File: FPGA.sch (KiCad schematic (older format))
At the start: 55 parts, among them J1 Conn_02x07_Odd_Even, J2 26642801RP2, U3 XC7A100T-FTG256, U4 S25FL1, U5 SiT2024B, U6 AS6C1616

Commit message: Minor FPGA and MCU fixes
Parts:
- added C?: 100n, symbol Device:C
- U5: footprint Package_TO_SOT_SMD:SOT-23-5 -> Package_TO_SOT_SMD:SOT-23-5_HandSoldering
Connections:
- net +3V3: now also C?.2
- net GND: now also C?.1
- net done renamed DONE
- net program_b renamed PROGRAM_B
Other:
- moved on the sheet: U6
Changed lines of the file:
@@
 F 0 "U5" H 5183 4625 50  0000 C CNN
 F 1 "SiT2024B" H 5183 4534 50  0000 C CNN
-F 2 "Package_TO_SOT_SMD:SOT-23-5" H 5100 4500 50  0001 C CNN
+F 2 "Package_TO_SOT_SMD:SOT-23-5_HandSoldering" H 5100 4500 50  0001 C CNN
 F 3 "" H 5100 4500 50  0001 C CNN
 	1    5300 4550
@@
 	1    0    0    -1
 $EndComp
-Text Label 19250 3400 2    50   ~ 0
+Text Label 18300 4000 2    50   ~ 0
 SRAM_dio0
-Text Label 19250 3300 2    50   ~ 0
+Text Label 18300 3900 2    50   ~ 0
 SRAM_dio1
-Text Label 19250 3200 2    50   ~ 0
+Text Label 18300 3800 2    50   ~ 0
 SRAM_dio2
-Text Label 19250 3100 2    50   ~ 0
+Text Label 18300 3700 2    50   ~ 0
 SRAM_dio3
-Text Label 19250 3000 2    50   ~ 0
+Text Label 18300 3600 2    50   ~ 0
 SRAM_dio4
-Text Label 19250 2900 2    50   ~ 0
+Text Label 18300 3500 2    50   ~ 0
 SRAM_dio5
-Text Label 19250 2800 2    50   ~ 0
+Text Label 18300 3400 2    50   ~ 0
 SRAM_dio6
-Text Label 19250 2700 2    50   ~ 0
+Text Label 18300 3300 2    50   ~ 0
 SRAM_dio7
-Text Label 19250 2600 2    50   ~ 0
+Text Label 18300 3200 2    50   ~ 0
 SRAM_dio8
-Text Label 19250 2500 2    50   ~ 0
+Text Label 18300 3100 2    50   ~ 0
 SRAM_dio9
-Text Label 19250 2400 2    50   ~ 0
+Text Label 18300 3000 2    50   ~ 0
 SRAM_dio10
-Text Label 19250 2300 2    50   ~ 0
+Text Label 18300 2900 2    50   ~ 0
 SRAM_dio11
-Text Label 19250 2200 2    50   ~ 0
+Text Label 18300 2800 2    50   ~ 0
 SRAM_dio12
-Text Label 19250 2100 2    50   ~ 0
+Text Label 18300 2700 2    50   ~ 0
 SRAM_dio13
-Text Label 19250 2000 2    50   ~ 0
+Text Label 18300 2600 2    50   ~ 0
 SRAM_dio14
-Text Label 19250 1900 2    50   ~ 0
+Text Label 18300 2500 2    50   ~ 0
 SRAM_dio15
 Text Label 16650 2100 0    50   ~ 0
@@
 Text Label 16650 3600 0    50   ~ 0
 SRAM_dio15
-Text Label 20450 3800 0    50   ~ 0
+Text Label 19500 4400 0    50   ~ 0
 SRAM_a0
-Text Label 20450 3700 0    50   ~ 0
+Text Label 19500 4300 0    50   ~ 0
 SRAM_a1
-Text Label 20450 3600 0    50   ~ 0
+Text Label 19500 4200 0    50   ~ 0
 SRAM_a2
-Text Label 20450 3500 0    50   ~ 0
+Text Label 19500 4100 0    50   ~ 0
 SRAM_a3
-Text Label 20450 3400 0    50   ~ 0
+Text Label 19500 4000 0    50   ~ 0
 SRAM_a4
-Text Label 20450 3300 0    50   ~ 0
+Text Label 19500 3900 0    50   ~ 0
 SRAM_a5
-Text Label 20450 3200 0    50   ~ 0
+Text Label 19500 3800 0    50   ~ 0
 SRAM_a6
-Text Label 20450 3100 0    50   ~ 0
+Text Label 19500 3700 0    50   ~ 0
 SRAM_a7
-Text Label 20450 3000 0    50   ~ 0
+Text Label 19500 3600 0    50   ~ 0
 SRAM_a8
-Text Label 20450 2900 0    50   ~ 0
+Text Label 19500 3500 0    50   ~ 0
 SRAM_a9
-Text Label 20450 2800 0    50   ~ 0
+Text Label 19500 3400 0    50   ~ 0
 SRAM_a10
-Text Label 20450 2700 0    50   ~ 0
+Text Label 19500 3300 0    50   ~ 0
 SRAM_a11
-Text Label 20450 2600 0    50   ~ 0
+Text Label 19500 3200 0    50   ~ 0
 SRAM_a12
-Text Label 20450 2500 0    50   ~ 0
+Text Label 19500 3100 0    50   ~ 0
 SRAM_a13
-Text Label 20450 2400 0    50   ~ 0
+Text Label 19500 3000 0    50   ~ 0
 SRAM_a14
-Text Label 20450 2300 0    50   ~ 0
+Text Label 19500 2900 0    50   ~ 0
 SRAM_a15
-Text Label 20450 2200 0    50   ~ 0
+Text Label 19500 2800 0    50   ~ 0
 SRAM_a16
-Text Label 20450 2100 0    50   ~ 0
+Text Label 19500 2700 0    50   ~ 0
 SRAM_a17
-Text Label 20450 2000 0    50   ~ 0
+Text Label 19500 2600 0    50   ~ 0
 SRAM_a18
-Text Label 20450 1900 0    50   ~ 0
+Text Label 19500 2500 0    50   ~ 0
 SRAM_a19
 Text Label 16650 3700 0    50   ~ 0
@@
 L Memory_RAM:AS6C1616 U?
 U 1 1 5E505DC8
-P 19850 3000
+P 18900 3600
 AR Path="/5D7D43D9/5E0EF1ED/5E505DC8" Ref="U?"  Part="1"
 AR Path="/5D7D43D9/5E505DC8" Ref="U6"  Part="1"
-F 0 "U6" H 19600 4300 50  0000 C CNN
-F 1 "AS6C1616" H 20150 1700 50  0000 C CNN
-F 2 "Package_SO:TSOP-I-48_18.4x12mm_P0.5mm" H 20900 1650 50  0001 C CNN
-F 3 "https://www.alliancememory.com/wp-content/uploads/pdf/AS6C1616-TSOPI.pdf" H 19550 3450 50  0001 C CNN
-	1    19850 3000
-	1    0    0    -1
-$EndComp
-Text Label 19250 3600 2    50   ~ 0
+F 0 "U6" H 18650 4900 50  0000 C CNN
+F 1 "AS6C1616" H 19200 2300 50  0000 C CNN
+F 2 "Package_SO:TSOP-I-48_18.4x12mm_P0.5mm" H 19950 2250 50  0001 C CNN
+F 3 "https://www.alliancememory.com/wp-content/uploads/pdf/AS6C1616-TSOPI.pdf" H 18600 4050 50  0001 C CNN
+	1    18900 3600
+	1    0    0    -1
+$EndComp
+Text Label 18300 4200 2    50   ~ 0
 SRAM_oe#
-Text Label 19250 3700 2    50   ~ 0
+Text Label 18300 4300 2    50   ~ 0
 SRAM_we#
-Text Label 19250 3800 2    50   ~ 0
+Text Label 18300 4400 2    50   ~ 0
 SRAM_ce#
-Text Label 19250 3900 2    50   ~ 0
+Text Label 18300 4500 2    50   ~ 0
 SRAM_ce2
-Text Label 19250 4000 2    50   ~ 0
+Text Label 18300 4600 2    50   ~ 0
 SRAM_ub#
-Text Label 19250 4100 2    50   ~ 0
+Text Label 18300 4700 2    50   ~ 0
 SRAM_lb#
 Text Label 16650 5700 0    50   ~ 0
@@
 SRAM_lb#
 Wire Wire Line
-	19850 1400 19850 1600
+	18900 2000 18900 2100
 $Comp
 L power:GND #PWR?
 U 1 1 5E505DDB
-P 19450 4450
+P 18500 5050
 AR Path="/5D7D43D9/5E0EF1ED/5E505DDB" Ref="#PWR?"  Part="1"
 AR Path="/5D7D43D9/5E505DDB" Ref="#PWR0126"  Part="1"
-F 0 "#PWR0126" H 19450 4200 50  0001 C CNN
-F 1 "GND" H 19455 4277 50  0000 C CNN
-F 2 "" H 19450 4450 50  0001 C CNN
-F 3 "" H 19450 4450 50  0001 C CNN
-	1    19450 4450
-	1    0    0    -1
-$EndComp
-Wire Wire Line
-	19850 4400 19750 4400
-Wire Wire Line
-	19450 4400 19450 4450
-Connection ~ 19750 4400
-Wire Wire Line
-	19750 4400 19450 4400
+F 0 "#PWR0126" H 18500 4800 50  0001 C CNN
+F 1 "GND" H 18505 4877 50  0000 C CNN
+F 2 "" H 18500 5050 50  0001 C CNN
+F 3 "" H 18500 5050 50  0001 C CNN
+	1    18500 5050
+	1    0    0    -1
+$EndComp
+Wire Wire Line
+	18900 5000 18800 5000
+Wire Wire Line
+	18500 5000 18500 5050
+Connection ~ 18800 5000
+Wire Wire Line
+	18800 5000 18500 5000
 NoConn ~ 16650 6300
 NoConn ~ 16650 6400
@@
 L power:+3V3 #PWR?
 U 1 1 5E505DED
-P 19850 1400
+P 18900 2000
 AR Path="/5D7D43D9/5E0EF1ED/5E505DED" Ref="#PWR?"  Part="1"
 AR Path="/5D7D43D9/5E505DED" Ref="#PWR0127"  Part="1"
-F 0 "#PWR0127" H 19850 1250 50  0001 C CNN
-F 1 "+3V3" H 19865 1573 50  0000 C CNN
-F 2 "" H 19850 1400 50  0001 C CNN
-F 3 "" H 19850 1400 50  0001 C CNN
-	1    19850 1400
+F 0 "#PWR0127" H 18900 1850 50  0001 C CNN
+F 1 "+3V3" H 18915 2173 50  0000 C CNN
+F 2 "" H 18900 2000 50  0001 C CNN
+F 3 "" H 18900 2000 50  0001 C CNN
+	1    18900 2000
 	1    0    0    -1
 $EndComp
@@
 Connection ~ -1500 1050
 Connection ~ -1500 1850
-Text GLabel -2600 1600 3    50   Input ~ 0
-done
 Wire Wire Line
 	-2600 1250 -2600 1600
 Connection ~ -2600 1250
-Text GLabel -3200 1600 3    50   Input ~ 0
-program_b
 Wire Wire Line
 	-3200 1600 -3200 1450
@@
 Text HLabel 6700 3400 0    50   Input ~ 0
 MISO
+Text HLabel -3200 1600 3    50   Input ~ 0
+PROGRAM_B
+Text HLabel -2600 1600 3    50   Input ~ 0
+DONE
+$Comp
+L Device:C C?
+U 1 1 60BCCCE6
+P 19250 2100
+F 0 "C?" V 18998 2100 50  0000 C CNN
+F 1 "100n" V 19089 2100 50  0000 C CNN
+F 2 "" H 19288 1950 50  0001 C CNN
+F 3 "~" H 19250 2100 50  0001 C CNN
+	1    19250 2100
+	0    1    1    0
+$EndComp
+Wire Wire Line
+	19100 2100 18900 2100
+Connection ~ 18900 2100
+Wire Wire Line
+	18900 2100 18900 2200
+$Comp
+L power:GND #PWR?
+U 1 1 60BE3158
+P 19550 2100
+F 0 "#PWR?" H 19550 1850 50  0001 C CNN
+F 1 "GND" H 19555 1927 50  0000 C CNN
+F 2 "" H 19550 2100 50  0001 C CNN
+F 3 "" H 19550 2100 50  0001 C CNN
+	1    19550 2100
+	1    0    0    -1
+$EndComp
+Wire Wire Line
+	19550 2100 19400 2100
 $EndSCHEMATC

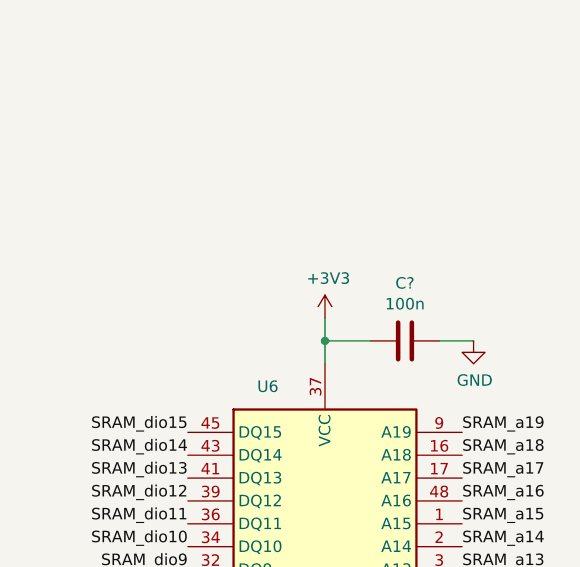
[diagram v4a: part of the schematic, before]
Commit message: Add various footprints
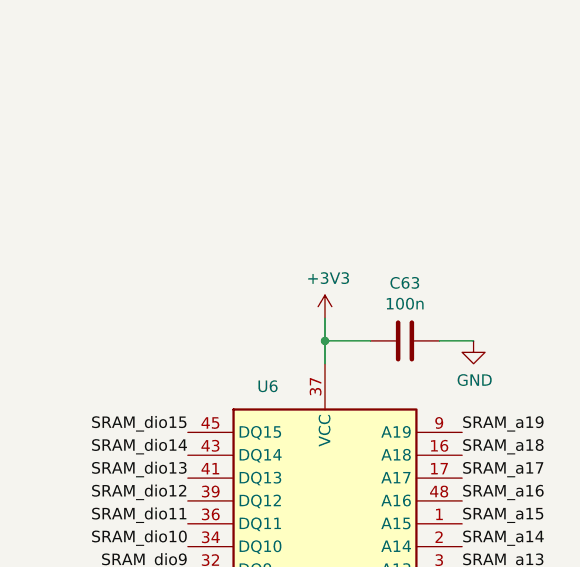
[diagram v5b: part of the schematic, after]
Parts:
- C20, C21, C22, C23, C24, C25, C26, C27, C28, C29, C30, C31, C32, C33, C34, C35, C36, C37, C38, C39, C40, C41, C42, C43, C44, C45, C46, C47, C48, C49, C50, C51, C52, C53, C54, C55, C56, C57, C58, C59, C60: footprint (none) -> Capacitor_SMD:C_1206_3216Metric_Pad1.42x1.75mm_HandSolder
- C63: renamed from C?; footprint (none) -> Capacitor_SMD:C_1206_3216Metric_Pad1.42x1.75mm_HandSolder
- J1: footprint (none) -> Connector_PinHeader_2.00mm:PinHeader_2x07_P2.00mm_Vertical_SMD
- R10, R11, R12, R13, R14, R15, R16, R17: footprint (none) -> Resistor_SMD:R_1206_3216Metric_Pad1.42x1.75mm_HandSolder
- U3: footprint (none) -> Package_BGA:Xilinx_FTG256

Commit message: Connect DAC/ADC to FPGA
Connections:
- net Audio I/O/SYSCLK: now reaches U3.L15 (IO_L3P_T0_DQS_PUDC_B_14)
- net ADC_DIN renamed Audio I/O/FPGAIn
- net BitClock renamed Audio I/O/BITCLK
- net DAC_DOUT renamed Audio I/O/FPGAOut
- net SampleClock renamed Audio I/O/LRCLK
- no-connect marks 91 -> 90
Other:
- note added: "Vccint"
- moved on the sheet: C21, C22, C23, C24, C26, C27, C28, C29, C30, C31, C32, C33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

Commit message: Fix pin headers
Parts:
- J2: footprint CON28_2X14_HDR_2664 -> Connector_PinHeader_2.54mm:PinHeader_2x14_P2.54mm_Vertical
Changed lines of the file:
@@
 F 0 "J2" H 4850 9187 60  0000 C CNN
 F 1 "26642801RP2" H 4850 9081 60  0000 C CNN
-F 2 "CON28_2X14_HDR_2664" H 4850 9040 60  0001 C CNN
+F 2 "Connector_PinHeader_2.54mm:PinHeader_2x14_P2.54mm_Vertical" H 4850 9040 60  0001 C CNN
 F 3 "" H 3850 8800 60  0000 C CNN
 	1    3850 8800

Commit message: Organize components and fix minor issues
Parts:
- J1: footprint Connector_PinHeader_2.00mm:PinHeader_2x07_P2.00mm_Vertical_SMD -> Connector_PinHeader_2.00mm:PinHeader_2x07_P2.00mm_Vertical
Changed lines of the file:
@@
 F 0 "J1" H -4550 1567 50  0000 C CNN
 F 1 "Conn_02x07_Odd_Even" H -4550 1476 50  0000 C CNN
-F 2 "Connector_PinHeader_2.00mm:PinHeader_2x07_P2.00mm_Vertical_SMD" H -4600 1050 50  0001 C CNN
+F 2 "Connector_PinHeader_2.00mm:PinHeader_2x07_P2.00mm_Vertical" H -4600 1050 50  0001 C CNN
 F 3 "~" H -4600 1050 50  0001 C CNN
 	1    -4600 1050
